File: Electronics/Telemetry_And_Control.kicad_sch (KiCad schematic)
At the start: 4 parts, among them J1 Micro_SD_Card_Det_Hirose_DM3AT, U5 ESP32-S3-WROOM-1

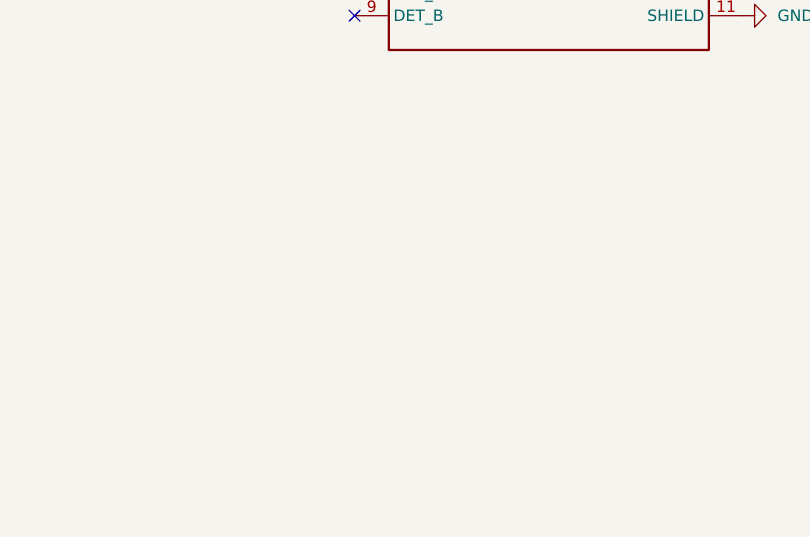
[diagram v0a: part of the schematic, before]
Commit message: CP2102-GM Symbol
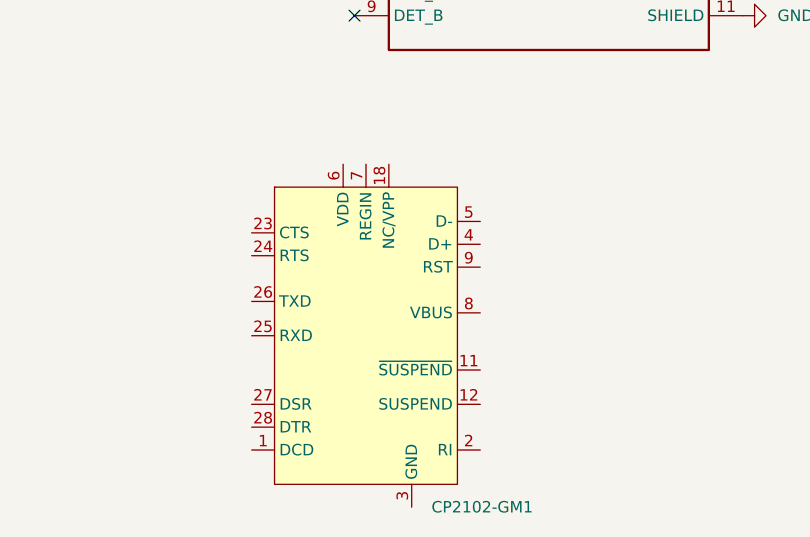
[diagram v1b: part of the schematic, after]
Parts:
- added CP2102-GM1: ~, Package_DFN_QFN:QFN-28-1EP_5x5mm_P0.5mm_EP3.1x3.1mm, symbol CP2102-GM:CP2102-GM
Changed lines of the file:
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@@
+    )
+  )
+  (symbol (lib_id "CP2102-GM:CP2102-GM") (at 137.16 116.84 0) (unit 1)
+    (in_bom yes) (on_board yes) (dnp no) (fields_autoplaced)
+    (property "Reference" "CP2102-GM1" (at 138.0841 121.92 0)
+      (effects (font (size 1.27 1.27)) (justify left))
+    )
+    (property "Value" "~" (at 134.62 116.84 0)
+      (effects (font (size 1.27 1.27)))
+    )
+    (property "Footprint" "Package_DFN_QFN:QFN-28-1EP_5x5mm_P0.5mm_EP3.1x3.1mm" (at 99.06 125.73 0)
+      (effects (font (size 1.27 1.27)) hide)
+    )
+    (property "Datasheet" "" (at 134.62 116.84 0)
+      (effects (font (size 1.27 1.27)) hide)
+    )
+    (pin "2")
+    (pin "23")
+    (pin "6")
+    (pin "12")
+    (pin "18")
+    (pin "11")
+    (pin "24")
+    (pin "1")
+    (pin "3")
+    (pin "26")
+    (pin "28")
+    (pin "27")
+    (pin "25")
+    (pin "8")
+    (pin "4")
+    (pin "9")
+    (pin "7")
+    (pin "5")
+    (instances
+      (project "Electronics"
+        (path "/4c70cac4-2e87-4919-a1c8-fe5f41acf493/28e49ffd-844b-4c36-9531-34600f6208a5"
+          (reference "CP2102-GM1") (unit 1)
+        )
+      )
     )
   )

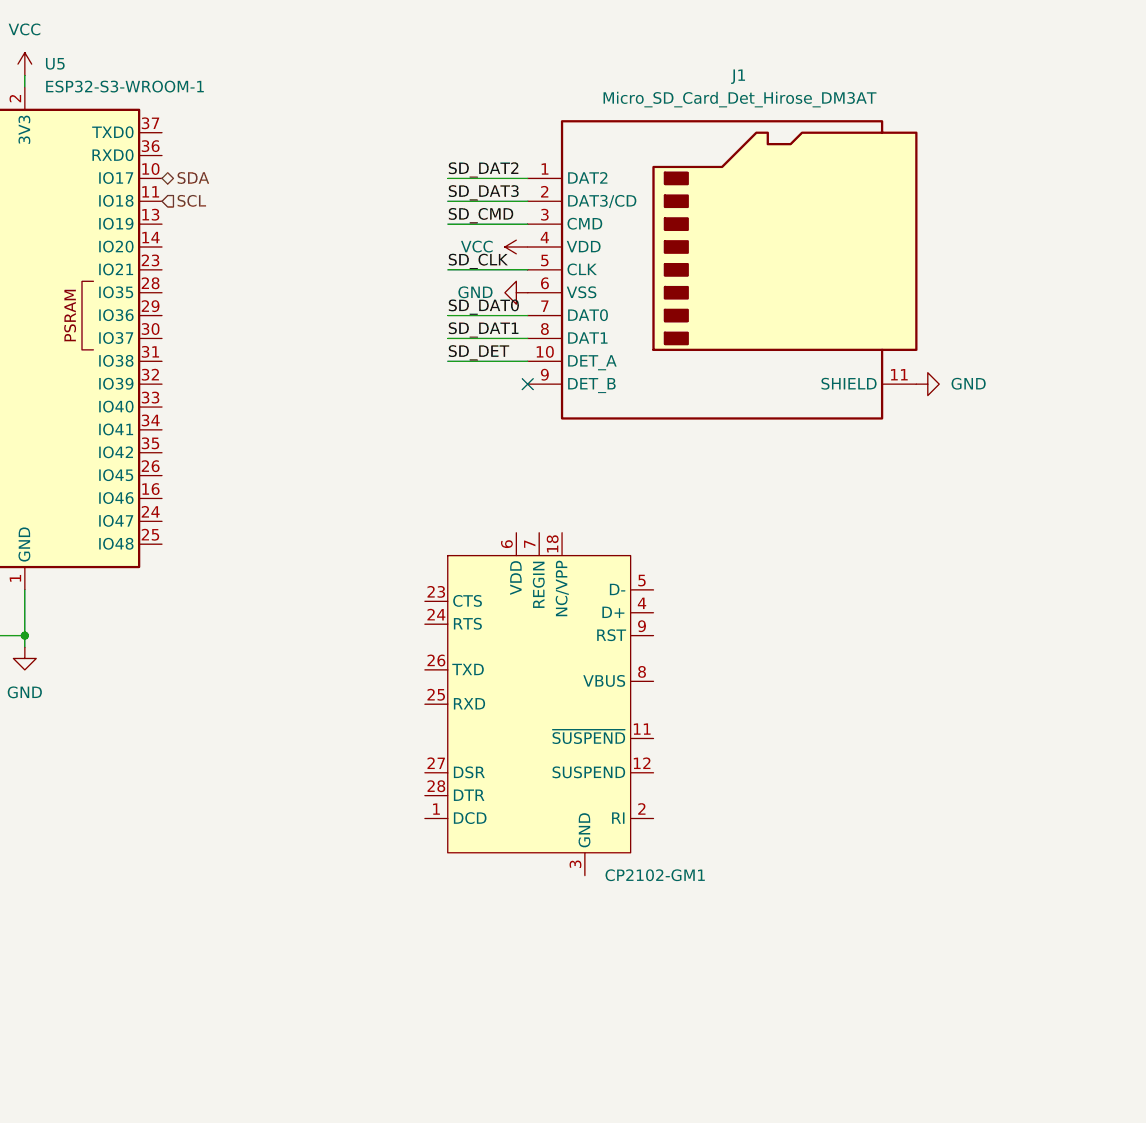
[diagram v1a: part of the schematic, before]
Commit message: USB to UART converter
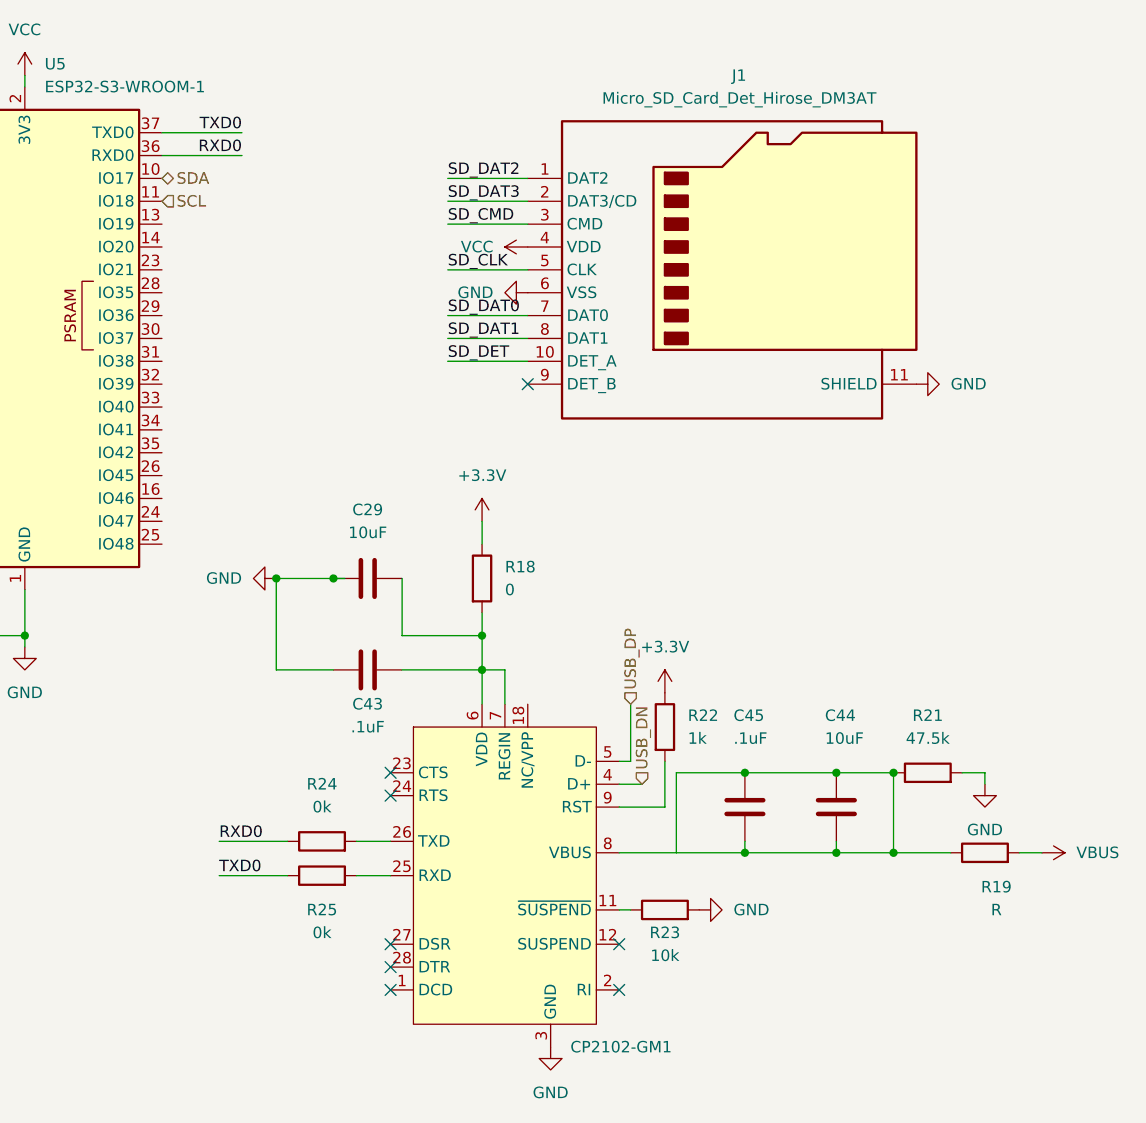
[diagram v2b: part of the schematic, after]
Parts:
- added C29, C44: 10uF, symbol Device:C
- added C43, C45: .1uF, symbol Device:C
- added R18: 0, symbol Device:R
- added R19: R, symbol Device:R
- added R21: 47.5k, symbol Device:R
- added R22: 1k, symbol Device:R
- added R23: 10k, symbol Device:R
- added R24, R25: 0k, symbol Device:R
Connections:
- net GND: now also CP2102-GM1.3 (GND), C29.1, C43.2, R21.2, R23.2
- net at CP2102-GM1.11 (~{SUSPEND}): now also R23.1
- net at CP2102-GM1.25 (RXD): now also R25.2
- net at CP2102-GM1.26 (TXD): now also R24.2
- net USB_DN: now reaches CP2102-GM1.4 (D+)
- net USB_DP: now reaches CP2102-GM1.5 (D-)
- net at CP2102-GM1.6 (VDD): now also CP2102-GM1.7 (REGIN), C29.2, C43.1, R18.2
- net at CP2102-GM1.8 (VBUS): now also C44.1, C44.2, C45.1, C45.2, R19.1, R21.1
- net at CP2102-GM1.9 (RST): now also R22.2
- net RXD0: now reaches U5.36 (RXD0)
- net RXD0: now also R24.1
- net TXD0: now reaches U5.37 (TXD0)
- net TXD0: now also R25.1
- new net +3.3V: R18.1, R22.1
- new net VBUS: R19.2
- no-connect marks 1 -> 8
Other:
- moved on the sheet: CP2102-GM1

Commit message: mostly done, needs review, needs pins
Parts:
- removed C29, C44: 10uF, symbol Device:C
- removed C43: .1uF, symbol Device:C
- removed CP2102-GM1: ~, Package_DFN_QFN:QFN-28-1EP_5x5mm_P0.5mm_EP3.1x3.1mm, symbol CP2102-GM:CP2102-GM
- removed R18: 0, symbol Device:R
- removed R19: R, symbol Device:R
- removed R21: 47.5k, symbol Device:R
- removed R25: 0k, symbol Device:R
- added C46: 100nF, symbol Device:C
- added SW6: SW_Push, symbol Switch:SW_Push
- added SW7: ~{USB_BOOT}, symbol Switch:SW_SPST
- C45: value .1uF -> 100nF
- R22: footprint (none) -> Resistor_SMD:R_0201_0603Metric
- R23: value 10k -> 1k; footprint (none) -> Resistor_SMD:R_0201_0603Metric
- R24: value 0k -> 1k; footprint (none) -> Resistor_SMD:R_0201_0603Metric
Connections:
- net +3.3V is gone; now on net VCC: R22.1
- net GND: now also C45.2, R23.1, C46.2, SW6.1, SW7.2 (B); no longer R23.2
- net VCC: now also R24.1
- net at C45.1: now also R22.2, U5.3 (EN), SW6.2; no longer C45.2
- net at R24.2: now also U5.27 (IO0), C46.1, SW7.1 (A)
- net USB-: now reaches U5.13 (IO19)
- net USB+: now reaches U5.14 (IO20)
- net at U5.16 (IO46): now also R23.2
- net RXD0: no longer names the net of U5.36 (RXD0)
- net RXD0: no longer R24.1
- net TXD0: no longer names the net of U5.37 (TXD0)
- no-connect marks 8 -> 24
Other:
- moved on the sheet: D1, J1, R1, U5

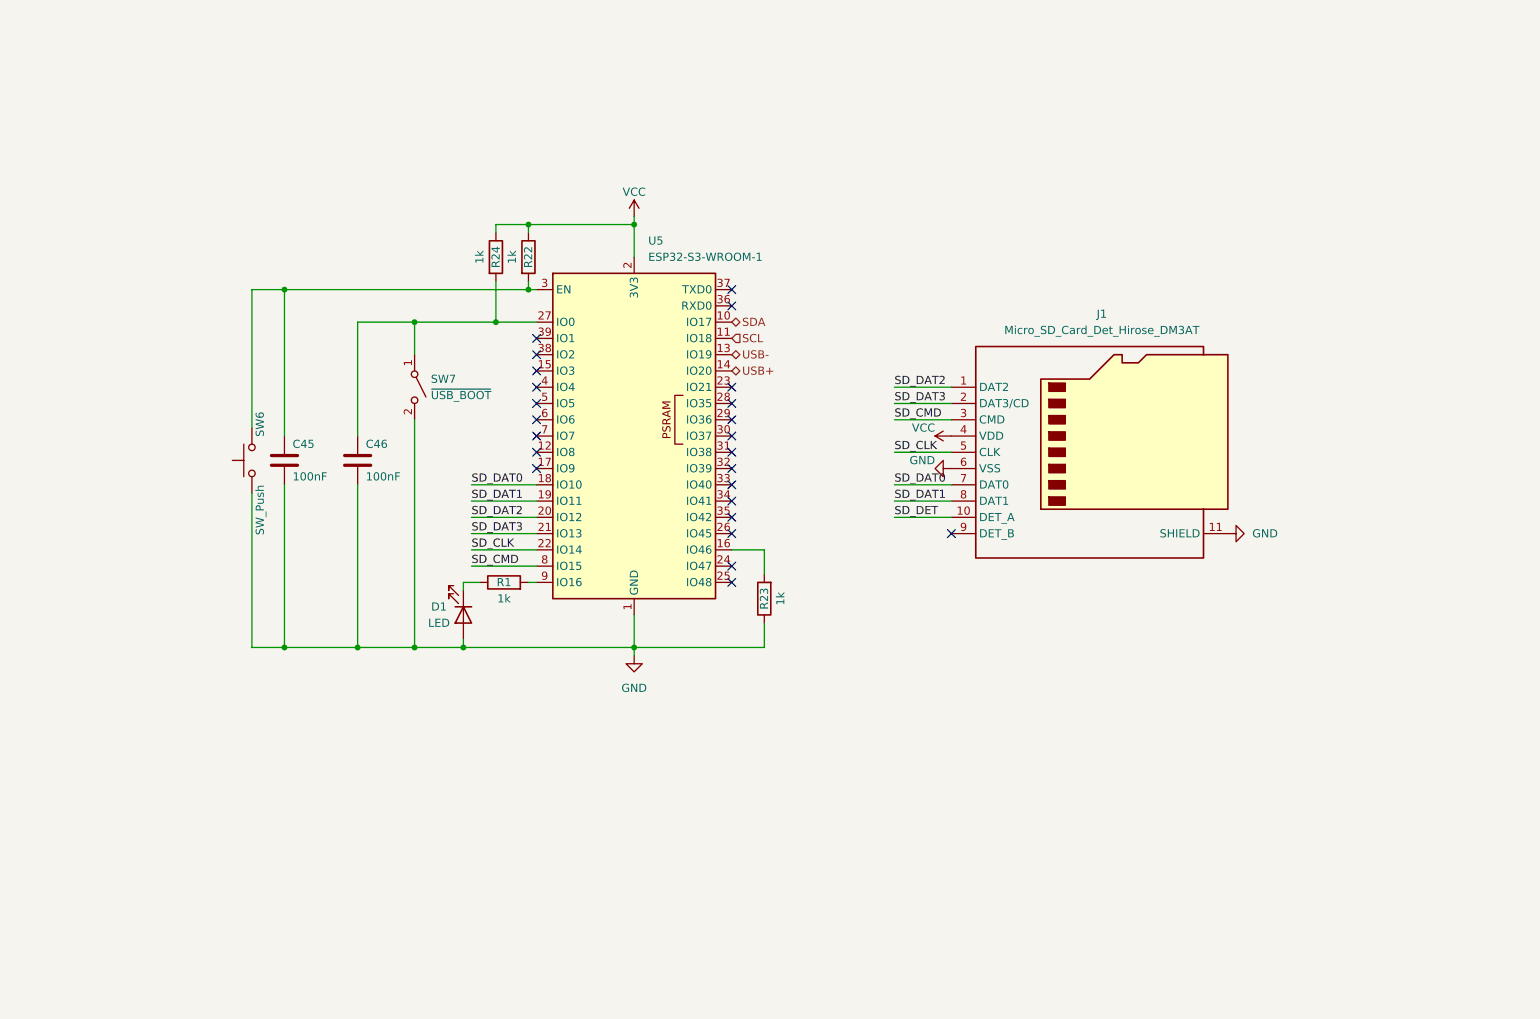
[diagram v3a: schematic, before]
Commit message: oled displays
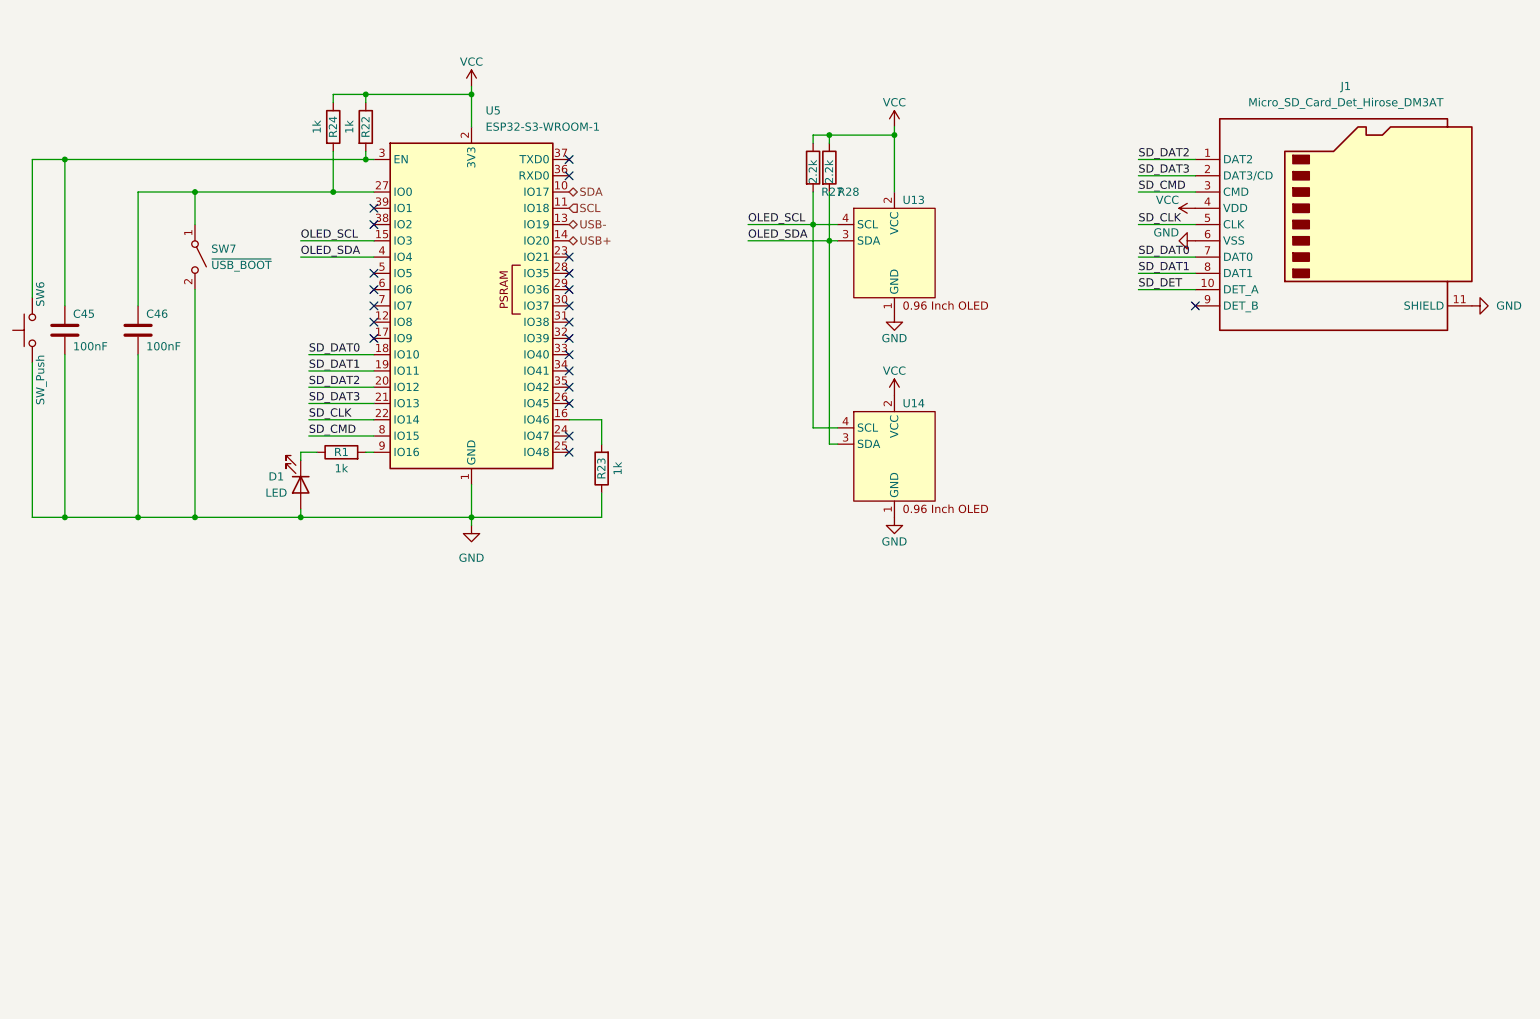
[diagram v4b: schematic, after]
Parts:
- added R27, R28: 2.2k, symbol Device:R
- added U13, U14: ~, Connector_PinHeader_2.54mm:PinHeader_1x04_P2.54mm_Vertical, symbol 0.96InchOLED:0.96_Inch_OLED
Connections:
- net GND: now also U13.1 (GND), U14.1 (GND)
- net VCC: now also R27.1, R28.1, U13.2 (VCC), U14.2 (VCC)
- net OLED_SCL: now reaches U5.15 (IO3)
- net OLED_SCL: now also R27.2, U13.4 (SCL), U14.4 (SCL)
- net OLED_SDA: now reaches U5.4 (IO4)
- net OLED_SDA: now also R28.2, U13.3 (SDA), U14.3 (SDA)
- no-connect marks 24 -> 22
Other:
- moved on the sheet: C45, C46, D1, J1, R1, R22, R23, R24, SW6, SW7, U5

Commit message: buttons
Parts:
- added R29, R30, R31, R32, R33, R34, R35, R36: 1k, Resistor_SMD:R_0201_0603Metric, symbol Device:R
- added SW10, SW11, SW12, SW13, SW14, SW15, SW8, SW9: SW_Push, symbol Switch:SW_Push
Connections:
- net GND: now also R29.1, R30.1, R31.1, R32.1, R33.1, R34.1, R35.1, R36.1
- net VCC: now also SW10.1, SW11.1, SW12.1, SW13.1, SW14.1, SW15.1, SW8.1, SW9.1
- net BTN0: now reaches U5.23 (IO21)
- net BTN0: now also R36.2, SW8.2
- net BTN7: now reaches U5.24 (IO47)
- net BTN7: now also R29.2, SW15.2
- net BTN6: now reaches U5.26 (IO45)
- net BTN6: now also R30.2, SW14.2
- net BTN1: now reaches U5.31 (IO38)
- net BTN1: now also R35.2, SW9.2
- net BTN2: now reaches U5.32 (IO39)
- net BTN2: now also R34.2, SW10.2
- net BTN3: now reaches U5.33 (IO40)
- net BTN3: now also R33.2, SW11.2
- net BTN4: now reaches U5.34 (IO41)
- net BTN4: now also R32.2, SW12.2
- net BTN5: now reaches U5.35 (IO42)
- net BTN5: now also R31.2, SW13.2
- net READY1: now reaches U5.5 (IO5)
- net READY2: now reaches U5.6 (IO6)
- no-connect marks 22 -> 12
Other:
- moved on the sheet: R23

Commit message: started pcb, need bigger frame
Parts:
- C45, C46: footprint (none) -> Capacitor_SMD:C_0201_0603Metric
- R27, R28: footprint (none) -> Resistor_SMD:R_0201_0603Metric
- SW10, SW11, SW12, SW13, SW14, SW15, SW6, SW8, SW9: footprint (none) -> Button_Switch_SMD:SW_SPST_TL3342
- SW7: footprint (none) -> Button_Switch_SMD:SW_DPDT_CK_JS202011JCQN
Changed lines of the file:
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@@
       (effects (font (size 1.27 1.27)))
     )
-    (property "Footprint" "" (at 63.5 123.19 0)
+    (property "Footprint" "Button_Switch_SMD:SW_SPST_TL3342" (at 63.5 123.19 0)
       (effects (font (size 1.27 1.27)) hide)
     )
@@
       (effects (font (size 1.27 1.27)) (justify left))
     )
-    (property "Footprint" "" (at 37.7952 80.01 0)
+    (property "Footprint" "Capacitor_SMD:C_0201_0603Metric" (at 37.7952 80.01 0)
       (effects (font (size 1.27 1.27)) hide)
     )
@@
       (effects (font (size 1.27 1.27)))
     )
-    (property "Footprint" "" (at 63.5 138.43 0)
+    (property "Footprint" "Button_Switch_SMD:SW_SPST_TL3342" (at 63.5 138.43 0)
       (effects (font (size 1.27 1.27)) hide)
     )
@@
       (effects (font (size 1.27 1.27)) (justify left))
     )
-    (property "Footprint" "" (at 57.15 64.77 0)
+    (property "Footprint" "Button_Switch_SMD:SW_DPDT_CK_JS202011JCQN" (at 57.15 64.77 0)
       (effects (font (size 1.27 1.27)) hide)
     )
@@
       (effects (font (size 1.27 1.27)))
     )
-    (property "Footprint" "" (at 63.5 158.75 0)
+    (property "Footprint" "Button_Switch_SMD:SW_SPST_TL3342" (at 63.5 158.75 0)
       (effects (font (size 1.27 1.27)) hide)
     )
@@
       (effects (font (size 1.27 1.27)))
     )
-    (property "Footprint" "" (at 63.5 143.51 0)
+    (property "Footprint" "Button_Switch_SMD:SW_SPST_TL3342" (at 63.5 143.51 0)
       (effects (font (size 1.27 1.27)) hide)
     )
@@
       (effects (font (size 1.27 1.27)))
     )
-    (property "Footprint" "" (at 63.5 128.27 0)
+    (property "Footprint" "Button_Switch_SMD:SW_SPST_TL3342" (at 63.5 128.27 0)
       (effects (font (size 1.27 1.27)) hide)
     )
@@
       (effects (font (size 1.27 1.27)) (justify right))
     )
-    (property "Footprint" "" (at 26.67 76.2 0)
+    (property "Footprint" "Button_Switch_SMD:SW_SPST_TL3342" (at 26.67 76.2 0)
       (effects (font (size 1.27 1.27)) hide)
     )
@@
       (effects (font (size 1.27 1.27)) (justify left))
     )
-    (property "Footprint" "" (at 151.892 50.8 90)
+    (property "Footprint" "Resistor_SMD:R_0201_0603Metric" (at 151.892 50.8 90)
       (effects (font (size 1.27 1.27)) hide)
     )
@@
       (effects (font (size 1.27 1.27)) (justify left))
     )
-    (property "Footprint" "" (at 154.432 50.8 90)
+    (property "Footprint" "Resistor_SMD:R_0201_0603Metric" (at 154.432 50.8 90)
       (effects (font (size 1.27 1.27)) hide)
     )
@@
       (effects (font (size 1.27 1.27)) (justify left))
     )
-    (property "Footprint" "" (at 49.2252 80.01 0)
+    (property "Footprint" "Capacitor_SMD:C_0201_0603Metric" (at 49.2252 80.01 0)
       (effects (font (size 1.27 1.27)) hide)
     )
@@
       (effects (font (size 1.27 1.27)))
     )
-    (property "Footprint" "" (at 63.5 133.35 0)
+    (property "Footprint" "Button_Switch_SMD:SW_SPST_TL3342" (at 63.5 133.35 0)
       (effects (font (size 1.27 1.27)) hide)
     )
@@
       (effects (font (size 1.27 1.27)))
     )
-    (property "Footprint" "" (at 63.5 148.59 0)
+    (property "Footprint" "Button_Switch_SMD:SW_SPST_TL3342" (at 63.5 148.59 0)
       (effects (font (size 1.27 1.27)) hide)
     )
@@
       (effects (font (size 1.27 1.27)))
     )
-    (property "Footprint" "" (at 63.5 153.67 0)
-      (effects (font (size 1.27 1.27)) hide)
-    )
+    (property "Footprint" "Button_Switch_SMD:SW_SPST_TL3342" (at 63.5 153.67 0)
+      (effects (font (size 1.27 1.27)) hide)
+    )
